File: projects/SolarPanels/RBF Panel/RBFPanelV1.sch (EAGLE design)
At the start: 43 parts

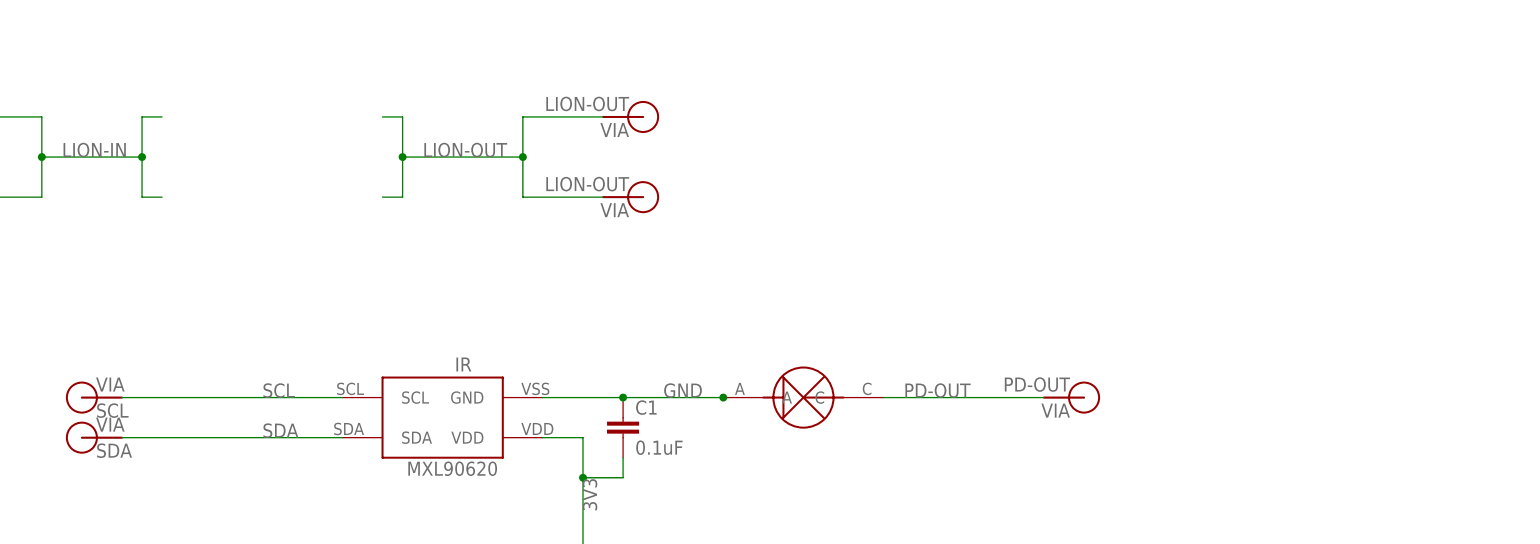
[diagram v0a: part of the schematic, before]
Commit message: Added RBF switches to library. (changed ABF to RBF) Added RBF switches and routing to RBF Panel. Vectorized all text on solar panel boards and rearranged as needed.
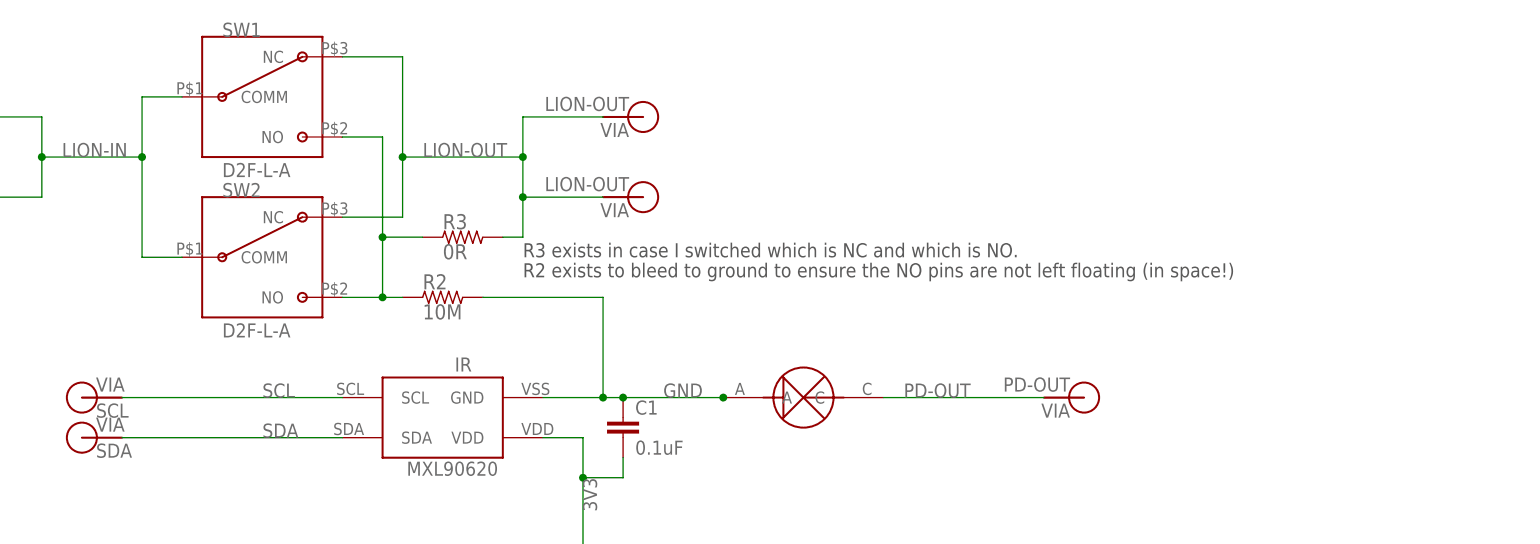
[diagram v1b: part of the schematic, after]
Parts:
- added R2: 10M, BrownSpaceEngineering:RES0805
- added R3: 0R, BrownSpaceEngineering:RES1210
- added SW1, SW2: D2F-L-A, BrownSpaceEngineering:D2F-L-A
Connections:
- new net N$13: R2.1, R3.1, SW1.NO, SW2.NO
- net GND: now also R2.2
- net LION-IN: now also SW1.COMM, SW2.COMM
- net LION-OUT: now also R3.2, SW1.NC, SW2.NC
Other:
- note added: "R2 exists to bleed to ground to ensure the NO pins are not left floating (in space!)"
- note added: "R3 exists in case I switched which is NC and which is NO."
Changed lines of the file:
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@@
 <part name="V3" library="BrownSpaceEngineering" deviceset="VIA" device="-60MIL" value="LION-OUT"/>
 <part name="V4" library="BrownSpaceEngineering" deviceset="VIA" device="-60MIL" value="LION-OUT"/>
+<part name="SW1" library="BrownSpaceEngineering" deviceset="D2F-L-A" device=""/>
+<part name="SW2" library="BrownSpaceEngineering" deviceset="D2F-L-A" device=""/>
+<part name="R2" library="BrownSpaceEngineering" deviceset="RES" device="0805" value="10M"/>
+<part name="R3" library="BrownSpaceEngineering" deviceset="RES" device="1210" value="0R"/>
 </parts>
 <sheets>
 <sheet>
 <plain>
+<text x="-68.58" y="124.46" size="1.778" layer="97">R3 exists in case I switched which is NC and which is NO.</text>
+<text x="-68.58" y="121.92" size="1.778" layer="97">R2 exists to bleed to ground to ensure the NO pins are not left floating (in space!)</text>
 </plain>
 <instances>
@@
 <instance part="V3" gate="G$1" x="-53.34" y="142.24" rot="R180"/>
 <instance part="V4" gate="G$1" x="-53.34" y="132.08" rot="R180"/>
+<instance part="SW1" gate="G$1" x="-101.6" y="144.78"/>
+<instance part="SW2" gate="G$1" x="-101.6" y="124.46"/>
+<instance part="R2" gate="R$1" x="-78.74" y="119.38"/>
+<instance part="R3" gate="R$1" x="-76.2" y="127"/>
 </instances>
 <busses>
@@
 <segment>
 <pinref part="IR" gate="G$1" pin="GND"/>
-<wire x1="-66.04" y1="106.68" x2="-55.88" y2="106.68" width="0.1524" layer="91"/>
+<wire x1="-66.04" y1="106.68" x2="-58.42" y2="106.68" width="0.1524" layer="91"/>
+<wire x1="-58.42" y1="106.68" x2="-55.88" y2="106.68" width="0.1524" layer="91"/>
 <wire x1="-55.88" y1="106.68" x2="-43.18" y2="106.68" width="0.1524" layer="91"/>
 <junction x="-43.18" y="106.68"/>
@@
 <pinref part="PD" gate="G$1" pin="A"/>
 <label x="-50.8" y="106.68" size="1.778" layer="95"/>
+<pinref part="R2" gate="R$1" pin="2"/>
+<wire x1="-73.66" y1="119.38" x2="-58.42" y2="119.38" width="0.1524" layer="91"/>
+<wire x1="-58.42" y1="119.38" x2="-58.42" y2="106.68" width="0.1524" layer="91"/>
+<junction x="-58.42" y="106.68"/>
 </segment>
 <segment>
@@
 <wire x1="-129.54" y1="137.16" x2="-116.84" y2="137.16" width="0.1524" layer="91"/>
 <junction x="-129.54" y="137.16"/>
-<wire x1="-116.84" y1="137.16" x2="-116.84" y2="142.24" width="0.1524" layer="91"/>
-<wire x1="-116.84" y1="142.24" x2="-114.3" y2="142.24" width="0.1524" layer="91"/>
-<wire x1="-116.84" y1="137.16" x2="-116.84" y2="132.08" width="0.1524" layer="91"/>
+<wire x1="-116.84" y1="137.16" x2="-116.84" y2="144.78" width="0.1524" layer="91"/>
 <junction x="-116.84" y="137.16"/>
-<wire x1="-116.84" y1="132.08" x2="-114.3" y2="132.08" width="0.1524" layer="91"/>
 <label x="-127" y="137.16" size="1.778" layer="95"/>
+<pinref part="SW1" gate="G$1" pin="COMM"/>
+<wire x1="-111.76" y1="144.78" x2="-116.84" y2="144.78" width="0.1524" layer="91"/>
+<pinref part="SW2" gate="G$1" pin="COMM"/>
+<wire x1="-111.76" y1="124.46" x2="-116.84" y2="124.46" width="0.1524" layer="91"/>
+<wire x1="-116.84" y1="124.46" x2="-116.84" y2="137.16" width="0.1524" layer="91"/>
 </segment>
 </net>
@@
 <wire x1="-68.58" y1="137.16" x2="-83.82" y2="137.16" width="0.1524" layer="91"/>
 <junction x="-68.58" y="137.16"/>
-<wire x1="-83.82" y1="137.16" x2="-83.82" y2="142.24" width="0.1524" layer="91"/>
-<wire x1="-83.82" y1="142.24" x2="-86.36" y2="142.24" width="0.1524" layer="91"/>
-<wire x1="-83.82" y1="137.16" x2="-83.82" y2="132.08" width="0.1524" layer="91"/>
+<wire x1="-83.82" y1="137.16" x2="-83.82" y2="129.54" width="0.1524" layer="91"/>
 <junction x="-83.82" y="137.16"/>
-<wire x1="-83.82" y1="132.08" x2="-86.36" y2="132.08" width="0.1524" layer="91"/>
 <label x="-81.28" y="137.16" size="1.778" layer="95"/>
-</segment>
-</net>
+<pinref part="SW2" gate="G$1" pin="NC"/>
+<wire x1="-91.44" y1="129.54" x2="-83.82" y2="129.54" width="0.1524" layer="91"/>
+<pinref part="SW1" gate="G$1" pin="NC"/>
+<wire x1="-91.44" y1="149.86" x2="-83.82" y2="149.86" width="0.1524" layer="91"/>
+<wire x1="-83.82" y1="149.86" x2="-83.82" y2="137.16" width="0.1524" layer="91"/>
+<pinref part="R3" gate="R$1" pin="2"/>
+<wire x1="-71.12" y1="127" x2="-68.58" y2="127" width="0.1524" layer="91"/>
+<wire x1="-68.58" y1="127" x2="-68.58" y2="132.08" width="0.1524" layer="91"/>
+<junction x="-68.58" y="132.08"/>
+</segment>
+</net>
+<net name="N$13" class="0">
+<segment>
+<pinref part="SW2" gate="G$1" pin="NO"/>
+<pinref part="R2" gate="R$1" pin="1"/>
+<wire x1="-91.44" y1="119.38" x2="-86.36" y2="119.38" width="0.1524" layer="91"/>
+<pinref part="SW1" gate="G$1" pin="NO"/>
+<wire x1="-86.36" y1="119.38" x2="-83.82" y2="119.38" width="0.1524" layer="91"/>
+<wire x1="-91.44" y1="139.7" x2="-86.36" y2="139.7" width="0.1524" layer="91"/>
+<wire x1="-86.36" y1="139.7" x2="-86.36" y2="127" width="0.1524" layer="91"/>
+<junction x="-86.36" y="119.38"/>
+<pinref part="R3" gate="R$1" pin="1"/>
+<wire x1="-86.36" y1="127" x2="-86.36" y2="119.38" width="0.1524" layer="91"/>
+<wire x1="-81.28" y1="127" x2="-86.36" y2="127" width="0.1524" layer="91"/>
+<junction x="-86.36" y="127"/>
+</segment>
+</net>
